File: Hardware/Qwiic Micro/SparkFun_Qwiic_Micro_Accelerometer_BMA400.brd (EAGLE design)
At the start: 7.6 x 19.1 mm, 40 parts, among them J1 QWIIC_RIGHT_ANGLE, U1 BMA400

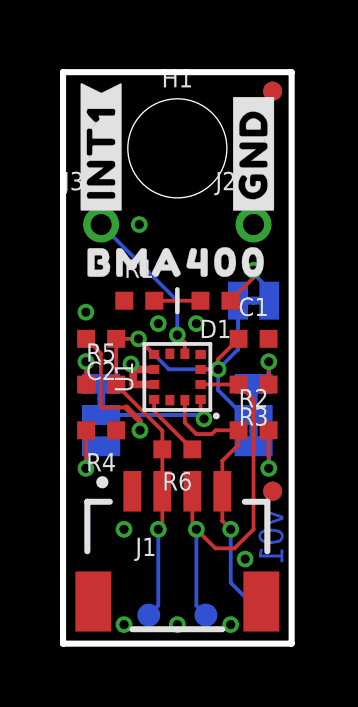
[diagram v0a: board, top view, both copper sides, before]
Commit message: Design review updates
Add BMA400 voltage range to schematics
Add designer name to boards' tDocu
Add measures to 1x1
Adjust traces of micro
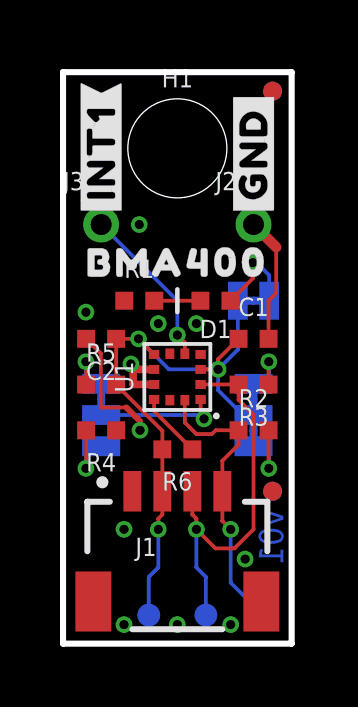
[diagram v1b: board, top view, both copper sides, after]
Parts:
- moved FRAME1 2.54 mm to (-19.1, -14.0)
- moved LOGO2 2.54 mm to (-19.1, -15.2)
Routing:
- net GND: track 6.54 -> 10.8 mm
- net N$1: track 2.57 -> 3.15 mm
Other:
- board text added: "Dryw Wade"
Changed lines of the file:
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@@
 <text x="6.9342" y="3.556" size="0.8128" layer="16" font="vector" ratio="20" rot="SMR270" align="center">v01</text>
 <rectangle x1="2.9972" y1="8.8646" x2="3.0734" y2="8.9154" layer="41"/>
+<text x="7.62" y="-13.97" size="1.778" layer="51" font="vector">Dryw Wade</text>
 </plain>
 <attributes>
@@
 <element name="FD3" library="SparkFun-Aesthetics" package="FIDUCIAL-MICRO" value="FIDUCIALUFIDUCIAL" x="6.985" y="18.415" smashed="yes"/>
 <element name="FD4" library="SparkFun-Aesthetics" package="FIDUCIAL-MICRO" value="FIDUCIALUFIDUCIAL" x="6.985" y="18.415" smashed="yes" rot="MR0"/>
-<element name="FRAME1" library="SparkFun-Aesthetics" package="CREATIVE_COMMONS" value="FRAME-LETTER" x="-19.05" y="-11.43" smashed="yes">
-<attribute name="DESIGNER" value="" x="60.96" y="-12.7" size="1.778" layer="27" display="off"/>
-<attribute name="REV" value="" x="60.96" y="-12.7" size="1.778" layer="27" display="off"/>
+<element name="FRAME1" library="SparkFun-Aesthetics" package="CREATIVE_COMMONS" value="FRAME-LETTER" x="-19.05" y="-13.97" smashed="yes">
+<attribute name="DESIGNER" value="" x="60.96" y="-15.24" size="1.778" layer="27" display="off"/>
+<attribute name="REV" value="" x="60.96" y="-15.24" size="1.778" layer="27" display="off"/>
 </element>
 <element name="H1" library="SparkFun-Hardware" package="STAND-OFF" value="STAND-OFF" x="3.81" y="16.51" smashed="yes">
@@
 </element>
 <element name="LOGO1" library="SparkFun-Aesthetics" package="QWIIC_3MM" value="QWIIC_LOGO_3MM" x="3.81" y="4.953" smashed="yes" rot="MR0"/>
-<element name="LOGO2" library="SparkFun-Aesthetics" package="BLANK" value="SFE_LOGO_NAMEBLANK" x="-19.05" y="-12.7" smashed="yes"/>
+<element name="LOGO2" library="SparkFun-Aesthetics" package="BLANK" value="SFE_LOGO_NAMEBLANK" x="-19.05" y="-15.24" smashed="yes"/>
 <element name="LOGO3" library="SparkFun-Aesthetics" package="OSHW-LOGO-S" value="OSHW-LOGOS" x="3.81" y="2.667" smashed="yes" rot="MR0"/>
 <element name="PWR" library="SparkFun-Jumpers" package="SMT-JUMPER_2_NC_TRACE_SILK" package3d_urn="urn:adsk.eagle:package:39281/1" value="JUMPER-SMT_2_NC_TRACE_SILK" x="6.35" y="11.43" smashed="yes" rot="MR0">
@@
 <wire x1="3.035" y1="9.14" x2="2.5186" y2="9.14" width="0.254" layer="1"/>
 <wire x1="2.5186" y1="9.14" x2="2.3368" y2="9.3218" width="0.254" layer="1"/>
+<wire x1="6.35" y1="13.97" x2="7.104" y2="13.216" width="0.3556" layer="1"/>
+<wire x1="7.104" y1="13.216" x2="7.104" y2="11.684" width="0.127" layer="1"/>
+<wire x1="7.104" y1="11.684" x2="6.85" y2="11.43" width="0.127" layer="1"/>
+<wire x1="6.85" y1="11.43" x2="6.85" y2="10.16" width="0.127" layer="1"/>
 </signal>
 <signal name="3.3V">
@@
 <contactref element="PWR" pad="2"/>
 <contactref element="TP2" pad="1"/>
-<wire x1="3.31" y1="5.08" x2="3.31" y2="3.945" width="0.127" layer="1"/>
-<wire x1="3.31" y1="3.945" x2="3.175" y2="3.81" width="0.127" layer="1"/>
+<wire x1="3.31" y1="5.08" x2="3.31" y2="4.3006" width="0.127" layer="1"/>
+<wire x1="3.31" y1="4.3006" x2="3.175" y2="4.1656" width="0.127" layer="1"/>
+<wire x1="3.175" y1="4.1656" x2="3.175" y2="3.81" width="0.127" layer="1"/>
 <via x="3.175" y="3.81" extent="1-16" drill="0.3048"/>
-<wire x1="3.175" y1="3.81" x2="3.175" y2="1.27" width="0.127" layer="16"/>
-<wire x1="3.175" y1="1.27" x2="2.8575" y2="0.9525" width="0.127" layer="16"/>
+<wire x1="3.175" y1="3.81" x2="3.175" y2="2.54" width="0.127" layer="16"/>
+<wire x1="3.175" y1="2.54" x2="2.8575" y2="2.2225" width="0.127" layer="16"/>
+<wire x1="2.8575" y1="2.2225" x2="2.8575" y2="0.9525" width="0.127" layer="16"/>
 <contactref element="R6" pad="2"/>
 <wire x1="3.31" y1="5.08" x2="3.31" y2="6.477" width="0.127" layer="1"/>
@@
 <contactref element="R3" pad="2"/>
 <contactref element="TP3" pad="1"/>
-<wire x1="4.31" y1="5.08" x2="4.31" y2="3.945" width="0.127" layer="1"/>
-<wire x1="4.31" y1="3.945" x2="4.445" y2="3.81" width="0.127" layer="1"/>
+<wire x1="4.31" y1="5.08" x2="4.31" y2="4.3006" width="0.127" layer="1"/>
+<wire x1="4.445" y1="4.1656" x2="4.445" y2="3.81" width="0.127" layer="1"/>
+<wire x1="4.445" y1="4.1656" x2="4.31" y2="4.3006" width="0.127" layer="1"/>
 <via x="4.445" y="3.81" extent="1-16" drill="0.3048"/>
-<wire x1="4.445" y1="3.81" x2="4.445" y2="1.27" width="0.127" layer="16"/>
-<wire x1="4.445" y1="1.27" x2="4.7625" y2="0.9525" width="0.127" layer="16"/>
+<wire x1="4.445" y1="3.81" x2="4.445" y2="2.54" width="0.127" layer="16"/>
+<wire x1="4.7625" y1="2.2225" x2="4.445" y2="2.54" width="0.127" layer="16"/>
+<wire x1="4.7625" y1="2.2225" x2="4.7625" y2="0.9525" width="0.127" layer="16"/>
 <wire x1="4.445" y1="3.81" x2="5.08" y2="3.175" width="0.127" layer="1"/>
 <wire x1="5.715" y1="3.175" x2="5.08" y2="3.175" width="0.127" layer="1"/>
@@
 <wire x1="4.585" y1="8.64" x2="5.846" y2="8.64" width="0.127" layer="1"/>
 <wire x1="5.846" y1="8.64" x2="5.85" y2="8.636" width="0.127" layer="1"/>
-<wire x1="5.85" y1="8.636" x2="6.35" y2="8.136" width="0.127" layer="1"/>
-<wire x1="6.35" y1="8.136" x2="6.35" y2="3.81" width="0.127" layer="1"/>
+<wire x1="6.35" y1="7.628" x2="5.85" y2="8.128" width="0.127" layer="1"/>
+<wire x1="5.85" y1="8.636" x2="5.85" y2="8.128" width="0.127" layer="1"/>
+<wire x1="6.35" y1="7.628" x2="6.35" y2="3.81" width="0.127" layer="1"/>
 </signal>
 <signal name="ADR">
@@
 <contactref element="D1" pad="A"/>
 <contactref element="PWR" pad="1"/>
-<wire x1="6.35" y1="12.446" x2="6.35" y2="12.2" width="0.127" layer="1"/>
-<wire x1="6.35" y1="12.2" x2="5.58" y2="11.43" width="0.127" layer="1"/>
-<via x="6.35" y="12.446" extent="1-16" drill="0.3048"/>
-<wire x1="6.8707" y1="11.43" x2="6.8707" y2="11.811" width="0.127" layer="16"/>
-<wire x1="6.8707" y1="11.811" x2="6.35" y2="12.3317" width="0.127" layer="16"/>
-<wire x1="6.35" y1="12.446" x2="6.35" y2="12.3317" width="0.127" layer="16"/>
+<wire x1="6.3246" y1="12.7" x2="6.3246" y2="12.1746" width="0.127" layer="1"/>
+<wire x1="6.3246" y1="12.1746" x2="5.58" y2="11.43" width="0.127" layer="1"/>
+<via x="6.3246" y="12.7" extent="1-16" drill="0.3048"/>
+<wire x1="6.8707" y1="12.2809" x2="6.4516" y2="12.7" width="0.127" layer="16"/>
+<wire x1="6.3246" y1="12.7" x2="6.4516" y2="12.7" width="0.127" layer="16"/>
+<wire x1="6.8707" y1="12.2809" x2="6.8707" y2="11.43" width="0.127" layer="16"/>
 </signal>
 </signals>

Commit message: Design review updates
Reduce silk labels on top side of 1x1
Adjust position of "BMA400" top silk of Micro
Rotate PWR jumper of Micro
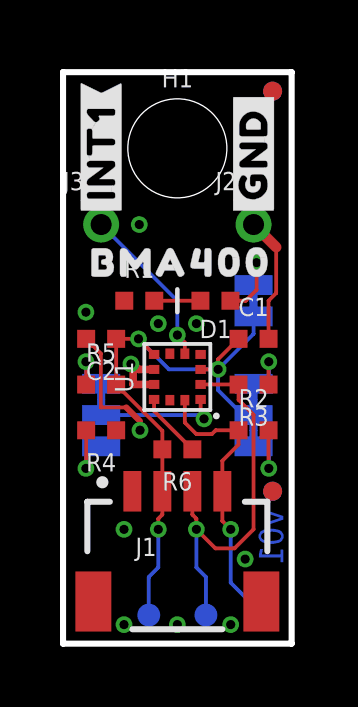
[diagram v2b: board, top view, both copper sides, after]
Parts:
- moved U$11 0.13 mm to (5.59, 11.4)
- moved U$5 0.13 mm to (3.94, 12.7)
- turned PWR to 270 degrees
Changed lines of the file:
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@@
 <layer number="38" name="bTest" color="7" fill="1" visible="no" active="yes"/>
 <layer number="39" name="tKeepout" color="4" fill="11" visible="yes" active="yes"/>
-<layer number="40" name="bKeepout" color="1" fill="11" visible="yes" active="yes"/>
+<layer number="40" name="bKeepout" color="1" fill="11" visible="no" active="yes"/>
 <layer number="41" name="tRestrict" color="4" fill="10" visible="yes" active="yes"/>
-<layer number="42" name="bRestrict" color="1" fill="10" visible="yes" active="yes"/>
-<layer number="43" name="vRestrict" color="2" fill="10" visible="yes" active="yes"/>
+<layer number="42" name="bRestrict" color="1" fill="10" visible="no" active="yes"/>
+<layer number="43" name="vRestrict" color="2" fill="10" visible="no" active="yes"/>
 <layer number="44" name="Drills" color="7" fill="1" visible="no" active="yes"/>
 <layer number="45" name="Holes" color="7" fill="1" visible="yes" active="yes"/>
-<layer number="46" name="Milling" color="3" fill="1" visible="yes" active="yes"/>
+<layer number="46" name="Milling" color="3" fill="1" visible="no" active="yes"/>
 <layer number="47" name="Measures" color="7" fill="1" visible="yes" active="yes"/>
 <layer number="48" name="Document" color="7" fill="1" visible="no" active="yes"/>
@@
 <layer number="50" name="dxf" color="7" fill="1" visible="no" active="no"/>
 <layer number="51" name="tDocu" color="6" fill="1" visible="yes" active="yes"/>
-<layer number="52" name="bDocu" color="7" fill="1" visible="yes" active="yes"/>
+<layer number="52" name="bDocu" color="7" fill="1" visible="no" active="yes"/>
 <layer number="53" name="tGND_GNDA" color="7" fill="9" visible="no" active="no"/>
 <layer number="54" name="bGND_GNDA" color="1" fill="9" visible="no" active="no"/>
@@
 <element name="LOGO2" library="SparkFun-Aesthetics" package="BLANK" value="SFE_LOGO_NAMEBLANK" x="-19.05" y="-15.24" smashed="yes"/>
 <element name="LOGO3" library="SparkFun-Aesthetics" package="OSHW-LOGO-S" value="OSHW-LOGOS" x="3.81" y="2.667" smashed="yes" rot="MR0"/>
-<element name="PWR" library="SparkFun-Jumpers" package="SMT-JUMPER_2_NC_TRACE_SILK" package3d_urn="urn:adsk.eagle:package:39281/1" value="JUMPER-SMT_2_NC_TRACE_SILK" x="6.35" y="11.43" smashed="yes" rot="MR0">
-<attribute name="NAME" x="6.35" y="12.573" size="0.6096" layer="26" font="vector" ratio="20" rot="MR0" align="bottom-center"/>
-<attribute name="VALUE" x="6.35" y="10.287" size="0.6096" layer="28" font="vector" ratio="20" rot="MR0" align="top-center"/>
+<element name="PWR" library="SparkFun-Jumpers" package="SMT-JUMPER_2_NC_TRACE_SILK" package3d_urn="urn:adsk.eagle:package:39281/1" value="JUMPER-SMT_2_NC_TRACE_SILK" x="6.35" y="11.43" smashed="yes" rot="MR270">
+<attribute name="NAME" x="5.207" y="11.43" size="0.6096" layer="26" font="vector" ratio="20" rot="MR270" align="bottom-center"/>
+<attribute name="VALUE" x="7.493" y="11.43" size="0.6096" layer="28" font="vector" ratio="20" rot="MR270" align="top-center"/>
 </element>
 <element name="R1" library="SparkFun-Resistors" package="0402-TIGHT" value="2.2k" x="2.54" y="11.43" smashed="yes">
@@
 <element name="U$4" library="output" package="#INT1#0" value="" x="1.27" y="14.097" smashed="yes" rot="MR90"/>
 <element name="LOGO4" library="SparkFun-Aesthetics" package="SFE_LOGO_FLAME_.1" value="SFE_LOGO_FLAME.1_INCH" x="3.81" y="13.335" smashed="yes" rot="MR0"/>
-<element name="U$5" library="output" package="BMA4000" value="" x="3.81" y="12.7" smashed="yes"/>
+<element name="U$5" library="output" package="BMA4000" value="" x="3.937" y="12.7" smashed="yes"/>
 <element name="U$7" library="output" package="#I2C#0" value="" x="4.826" y="7.62" smashed="yes" rot="MR90"/>
 <element name="U$8" library="output" package="#ADR#0" value="" x="2.794" y="7.62" smashed="yes" rot="MR90"/>
 <element name="U$9" library="output" package="#0X15#0" value="" x="1.27" y="9.017" smashed="yes" rot="MR90"/>
 <element name="U$10" library="output" package="#0X14#0" value="" x="1.27" y="6.223" smashed="yes" rot="MR90"/>
-<element name="U$11" library="output" package="#PWR#0" value="" x="5.461" y="11.43" smashed="yes" rot="MR0"/>
+<element name="U$11" library="output" package="#PWR#0" value="" x="5.588" y="11.43" smashed="yes" rot="MR0"/>
 </elements>
 <signals>
@@
 <wire x1="5.169" y1="9.144" x2="5.169" y2="9.479" width="0.127" layer="1"/>
 <wire x1="5.169" y1="9.479" x2="5.85" y2="10.16" width="0.127" layer="1"/>
-<wire x1="5.8293" y1="11.43" x2="5.8293" y2="9.8043" width="0.127" layer="16"/>
-<wire x1="5.8293" y1="9.8043" x2="5.169" y2="9.144" width="0.127" layer="16"/>
 <wire x1="3.531" y1="9.144" x2="5.169" y2="9.144" width="0.127" layer="16"/>
 <wire x1="1.77" y1="8.636" x2="1.77" y2="10.16" width="0.127" layer="1"/>
@@
 <via x="2.515" y="10.16" extent="1-16" drill="0.3048"/>
 <wire x1="2.515" y1="10.16" x2="3.531" y2="9.144" width="0.127" layer="16"/>
+<wire x1="6.35" y1="10.9093" x2="6.35" y2="10.325" width="0.127" layer="16"/>
+<wire x1="6.35" y1="10.325" x2="5.169" y2="9.144" width="0.127" layer="16"/>
 </signal>
 <signal name="SCL">
@@
 <contactref element="D1" pad="A"/>
 <contactref element="PWR" pad="1"/>
-<wire x1="6.3246" y1="12.7" x2="6.3246" y2="12.1746" width="0.127" layer="1"/>
-<wire x1="6.3246" y1="12.1746" x2="5.58" y2="11.43" width="0.127" layer="1"/>
-<via x="6.3246" y="12.7" extent="1-16" drill="0.3048"/>
-<wire x1="6.8707" y1="12.2809" x2="6.4516" y2="12.7" width="0.127" layer="16"/>
-<wire x1="6.3246" y1="12.7" x2="6.4516" y2="12.7" width="0.127" layer="16"/>
-<wire x1="6.8707" y1="12.2809" x2="6.8707" y2="11.43" width="0.127" layer="16"/>
+<wire x1="6.4516" y1="12.7" x2="6.4516" y2="11.7936" width="0.127" layer="1"/>
+<wire x1="6.4516" y1="11.7936" x2="6.088" y2="11.43" width="0.127" layer="1"/>
+<wire x1="6.088" y1="11.43" x2="5.58" y2="11.43" width="0.127" layer="1"/>
+<via x="6.4516" y="12.7" extent="1-16" drill="0.3048"/>
+<wire x1="6.35" y1="11.9507" x2="6.4516" y2="12.0523" width="0.127" layer="16"/>
+<wire x1="6.4516" y1="12.0523" x2="6.4516" y2="12.7" width="0.127" layer="16"/>
 </signal>
 </signals>
